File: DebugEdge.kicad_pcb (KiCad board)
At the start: 2 copper layers, 16 x 12 mm, 2 parts, among them J1 Upstream Host Connector, J2 DebugEdge_02x05

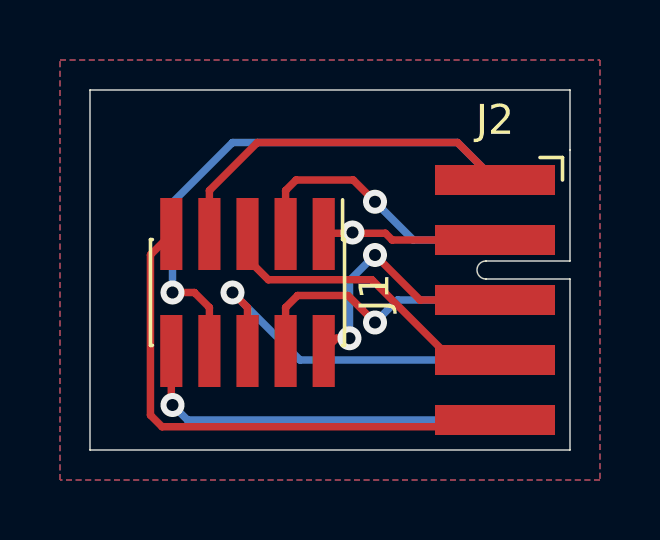
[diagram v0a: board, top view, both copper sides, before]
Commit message: Add solder bridge for Vref & BYOP pins.
BYOP in case you need to bring your own power!
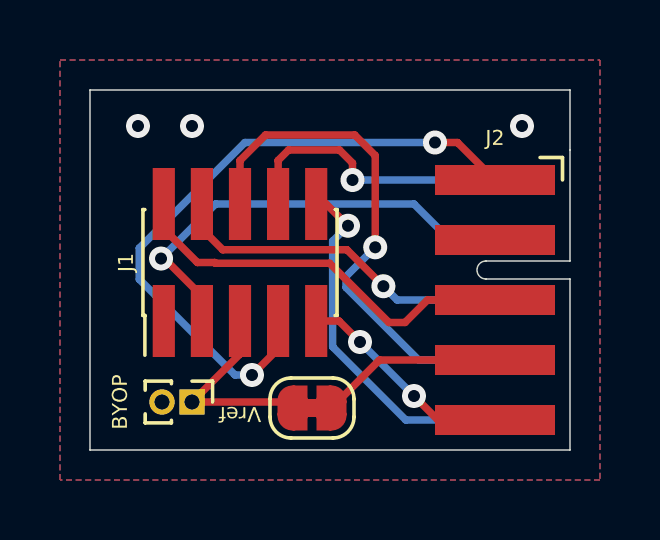
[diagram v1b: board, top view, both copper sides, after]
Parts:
- added J3: BYOP, Connector_PinHeader_1.00mm:PinHeader_1x02_P1.00mm_Vertical, F.Cu at (157.4, 98.4)
- added JP1: SolderJumper_2_Bridged, Jumper:SolderJumper-2_P1.3mm_Bridged_RoundedPad1.0x1.5mm, F.Cu at (161.4, 98.6)
- added Ref**: Val**, Connector_DebugEdge:DebugEdge_URL_Silk, B.Cu at (162.8, 95.6)
- moved J1 1.03 mm to (159.0, 93.8), turned to 90 degrees
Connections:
- J2 pad 5: VCC -> Net-(J2-Pad5)
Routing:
- net Net-(J1-Pad9): track 18.1 -> 7.33 mm, vias 0 -> 2
- net Net-(J1-Pad7): track 12.2 -> 22.1 mm, vias 0 -> 2
- net Net-(J1-Pad8): track 19.5 -> 9.57 mm
- net Net-(J2-Pad5): track 0.00 -> 6.11 mm
- net GND: track 5.81 -> 0.00 mm, vias 1 -> 3
- net Net-(J1-Pad6): track 11.8 -> 17.4 mm
- net /SWCLK: track 9.68 -> 15.1 mm
- net /SWDIO: track 8.78 -> 13.5 mm, vias 2 -> 0
- net VCC: track 10.5 -> 6.80 mm
- net /~RESET~: track 9.28 -> 11.6 mm
- net Net-(J1-Pad10): track 12.8 -> 12.1 mm
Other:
- board text added: "BYOP"
- board text added: "Revision 1"
- board text added: "Vref"
